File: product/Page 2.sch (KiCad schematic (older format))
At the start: 25 parts, among them J3 Conn_02x05_Odd_Even, Q1 Q_NMOS_GSD, Q2 Q_NMOS_GSD, Q3 Q_NMOS_GSD, SW1 SW_SPST, SW2 SW_SPST, U3 ESP32-WROOM-32D, X1 ECS-2520MV

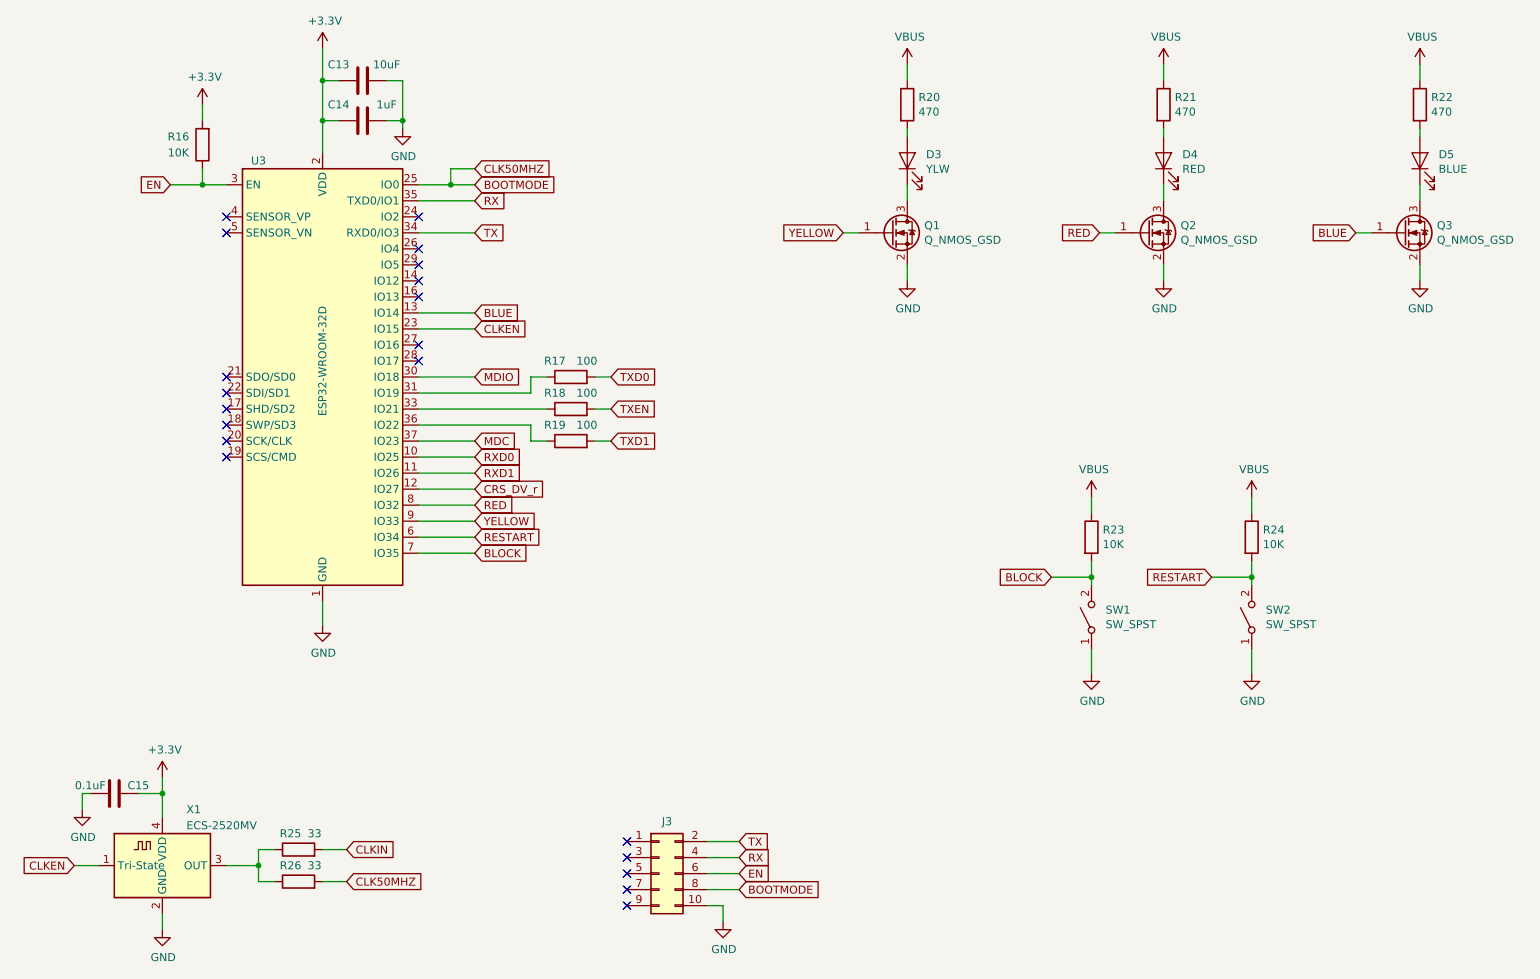
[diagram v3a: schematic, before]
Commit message: Removed oscillator, replaced with IO17
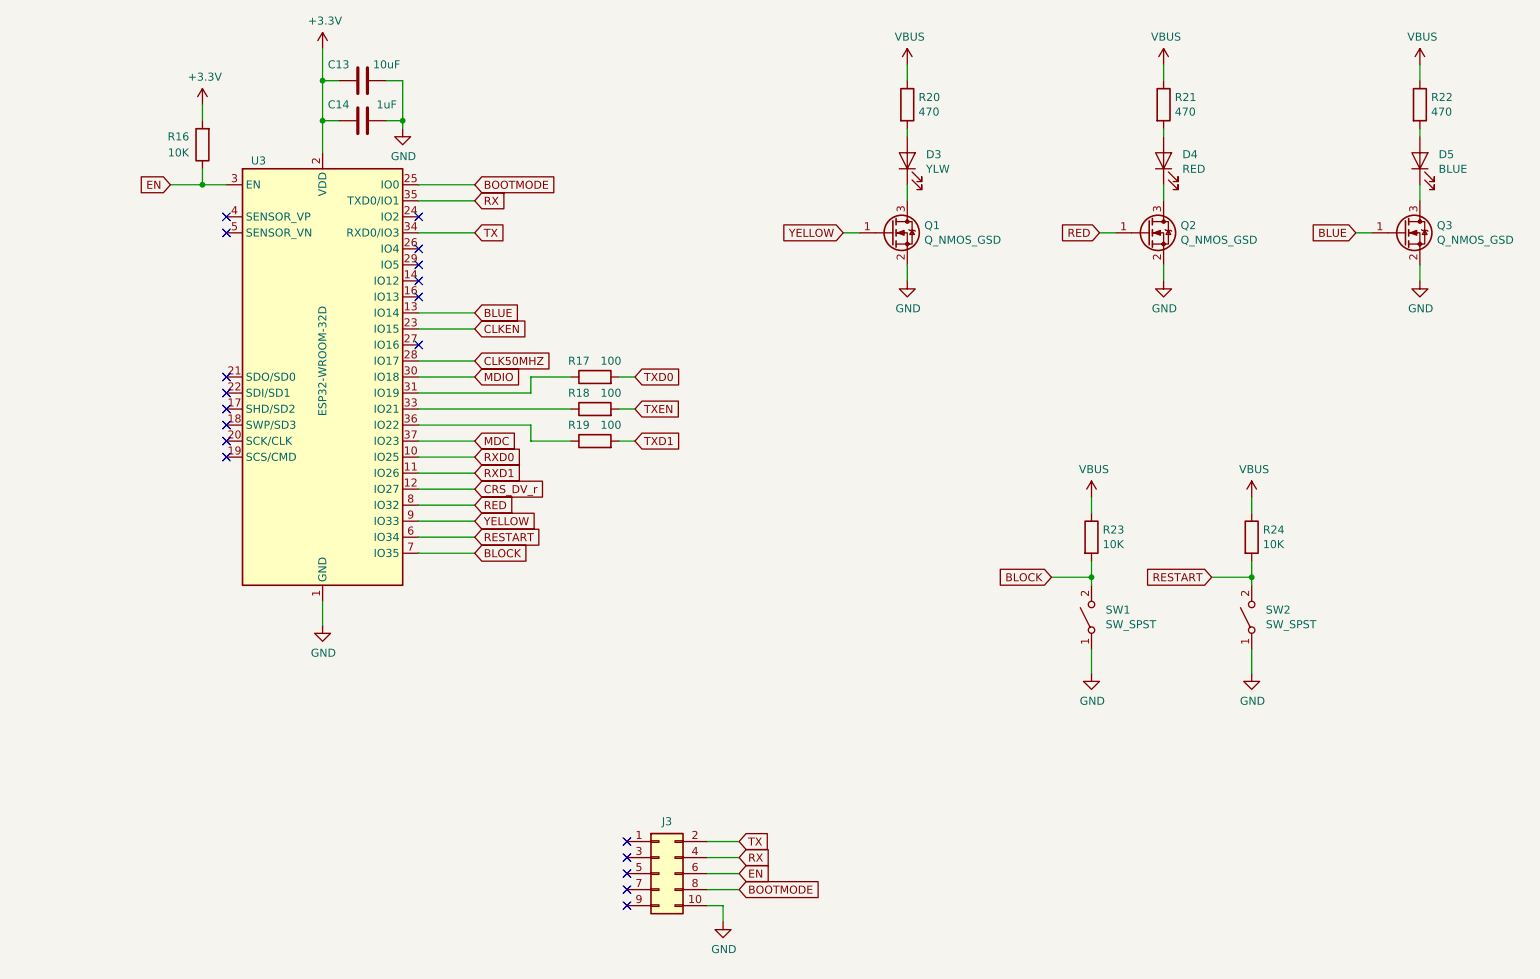
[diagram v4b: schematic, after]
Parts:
- removed C15: 0.1uF, Capacitor_SMD:C_0603_1608Metric, symbol Device:C
- removed R25, R26: 33, Resistor_SMD:R_0603_1608Metric, symbol Device:R
- removed X1: ECS-2520MV, Oscillator:Oscillator_SMD_ECS_2520MV-xxx-xx-4Pin_2.5x2.0mm, symbol Oscillator:ECS-2520MV-xxx-xx
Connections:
- net CLK50MHZ: now reaches U3.28 (IO17)
- no-connect marks 20 -> 19
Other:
- moved on the sheet: R17, R18, R19
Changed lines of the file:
@@
 $EndDescr
-$Comp
-L Oscillator:ECS-2520MV-xxx-xx X1
-U 1 1 5DF25907
-P 1900 6550
-F 0 "X1" H 2050 6900 50  0000 L CNN
-F 1 "ECS-2520MV" H 2050 6800 50  0000 L CNN
-F 2 "Oscillator:Oscillator_SMD_ECS_2520MV-xxx-xx-4Pin_2.5x2.0mm" H 2350 6200 50  0001 C CNN
-F 3 "https://www.ecsxtal.com/store/pdf/ECS-2520MV.pdf" H 1725 6675 50  0001 C CNN
-F 4 " C405472" H 1900 6550 50  0001 C CNN "LCSC Part Number"
-	1    1900 6550
-	1    0    0    -1
-$EndComp
 $Comp
 L EsperDNS-rescue:ESP32-WROOM-32D-RF_Module U3
@@
 Text GLabel 3850 4000 2    50   Input ~ 0
 RXD0
-Text GLabel 4700 3700 2    50   Input ~ 0
+Text GLabel 4850 3700 2    50   Input ~ 0
 TXEN
-Text GLabel 4700 3900 2    50   Input ~ 0
+Text GLabel 4850 3900 2    50   Input ~ 0
 TXD1
-Text GLabel 4700 3500 2    50   Input ~ 0
+Text GLabel 4850 3500 2    50   Input ~ 0
 TXD0
-Text GLabel 3050 6450 2    50   Input ~ 0
-CLKIN
 Text GLabel 3850 2400 2    50   Input ~ 0
 RX
@@
 Text GLabel 3850 2300 2    50   Input ~ 0
 BOOTMODE
-Text GLabel 3850 2200 2    50   Input ~ 0
+Text GLabel 3850 3400 2    50   Input ~ 0
 CLK50MHZ
 Text GLabel 3850 3100 2    50   Input ~ 0
@@
 L Device:R R18
 U 1 1 5DF2BBCB
-P 4450 3700
-F 0 "R18" V 4550 3800 50  0000 C CNN
-F 1 "100" V 4550 3600 50  0000 C CNN
-F 2 "Resistor_SMD:R_0603_1608Metric" V 4380 3700 50  0001 C CNN
-F 3 "~" H 4450 3700 50  0001 C CNN
-F 4 "C105588" H 4450 3700 50  0001 C CNN "LCSC Part Number"
-	1    4450 3700
+P 4600 3700
+F 0 "R18" V 4700 3800 50  0000 C CNN
+F 1 "100" V 4700 3600 50  0000 C CNN
+F 2 "Resistor_SMD:R_0603_1608Metric" V 4530 3700 50  0001 C CNN
+F 3 "~" H 4600 3700 50  0001 C CNN
+F 4 "C105588" H 4600 3700 50  0001 C CNN "LCSC Part Number"
+	1    4600 3700
 	0    -1   -1   0
 $EndComp
@@
 L Device:R R19
 U 1 1 5DF2BD63
-P 4450 3900
-F 0 "R19" V 4550 4000 50  0000 C CNN
-F 1 "100" V 4550 3800 50  0000 C CNN
-F 2 "Resistor_SMD:R_0603_1608Metric" V 4380 3900 50  0001 C CNN
-F 3 "~" H 4450 3900 50  0001 C CNN
-F 4 "C105588" H 4450 3900 50  0001 C CNN "LCSC Part Number"
-	1    4450 3900
-	0    -1   -1   0
-$EndComp
-Wire Wire Line
-	3500 2300 3700 2300
-Wire Wire Line
-	3700 2300 3700 2200
-Wire Wire Line
-	3700 2200 3850 2200
-Connection ~ 3700 2300
-Wire Wire Line
-	3700 2300 3850 2300
+P 4600 3900
+F 0 "R19" V 4700 4000 50  0000 C CNN
+F 1 "100" V 4700 3800 50  0000 C CNN
+F 2 "Resistor_SMD:R_0603_1608Metric" V 4530 3900 50  0001 C CNN
+F 3 "~" H 4600 3900 50  0001 C CNN
+F 4 "C105588" H 4600 3900 50  0001 C CNN "LCSC Part Number"
+	1    4600 3900
+	0    -1   -1   0
+$EndComp
 Wire Wire Line
 	3850 2600 3500 2600
@@
 	4200 3600 4200 3500
 Wire Wire Line
-	4200 3500 4300 3500
-Wire Wire Line
-	4300 3700 3500 3700
-Wire Wire Line
 	3500 3800 4200 3800
 Wire Wire Line
 	4200 3800 4200 3900
 Wire Wire Line
-	4200 3900 4300 3900
-Wire Wire Line
-	4600 3900 4700 3900
-Wire Wire Line
-	4600 3700 4700 3700
-Wire Wire Line
-	4700 3500 4600 3500
+	4750 3900 4850 3900
+Wire Wire Line
+	4750 3700 4850 3700
+Wire Wire Line
+	4850 3500 4750 3500
 Wire Wire Line
 	3500 3200 3850 3200
@@
 L Device:R R17
 U 1 1 5DF2A186
-P 4450 3500
-F 0 "R17" V 4550 3600 50  0000 C CNN
-F 1 "100" V 4550 3400 50  0000 C CNN
-F 2 "Resistor_SMD:R_0603_1608Metric" V 4380 3500 50  0001 C CNN
-F 3 "~" H 4450 3500 50  0001 C CNN
-F 4 "C105588" H 4450 3500 50  0001 C CNN "LCSC Part Number"
-	1    4450 3500
+P 4600 3500
+F 0 "R17" V 4700 3600 50  0000 C CNN
+F 1 "100" V 4700 3400 50  0000 C CNN
+F 2 "Resistor_SMD:R_0603_1608Metric" V 4530 3500 50  0001 C CNN
+F 3 "~" H 4600 3500 50  0001 C CNN
+F 4 "C105588" H 4600 3500 50  0001 C CNN "LCSC Part Number"
+	1    4600 3500
 	0    -1   -1   0
 $EndComp
@@
 	9450 2600 9350 2600
 $Comp
-L Device:R R25
-U 1 1 5DF75E2C
-P 2750 6450
-F 0 "R25" V 2850 6500 50  0000 C CNN
-F 1 "33" V 2850 6350 50  0000 C CNN
-F 2 "Resistor_SMD:R_0603_1608Metric" V 2680 6450 50  0001 C CNN
-F 3 "~" H 2750 6450 50  0001 C CNN
-F 4 "C417099" H 2750 6450 50  0001 C CNN "LCSC Part Number"
-	1    2750 6450
-	0    -1   -1   0
-$EndComp
-$Comp
-L Device:R R26
-U 1 1 5DF7703D
-P 2750 6650
-F 0 "R26" V 2850 6700 50  0000 C CNN
-F 1 "33" V 2850 6550 50  0000 C CNN
-F 2 "Resistor_SMD:R_0603_1608Metric" V 2680 6650 50  0001 C CNN
-F 3 "~" H 2750 6650 50  0001 C CNN
-F 4 "C417099" H 2750 6650 50  0001 C CNN "LCSC Part Number"
-	1    2750 6650
-	0    -1   -1   0
-$EndComp
-Text GLabel 3050 6650 2    50   Input ~ 0
-CLK50MHZ
-Wire Wire Line
-	2300 6550 2500 6550
-Wire Wire Line
-	2500 6550 2500 6450
-Wire Wire Line
-	2500 6450 2600 6450
-Wire Wire Line
-	2900 6450 3050 6450
-Wire Wire Line
-	3050 6650 2900 6650
-Wire Wire Line
-	2600 6650 2500 6650
-Wire Wire Line
-	2500 6650 2500 6550
-Connection ~ 2500 6550
-$Comp
-L power:GND #PWR0140
-U 1 1 5DF7E615
-P 1900 6950
-F 0 "#PWR0140" H 1900 6700 50  0001 C CNN
-F 1 "GND" H 1905 6777 50  0000 C CNN
-F 2 "" H 1900 6950 50  0001 C CNN
-F 3 "" H 1900 6950 50  0001 C CNN
-	1    1900 6950
-	1    0    0    -1
-$EndComp
-$Comp
-L power:+3.3V #PWR0141
-U 1 1 5DF7EA2D
-P 1900 6000
-F 0 "#PWR0141" H 1900 5850 50  0001 C CNN
-F 1 "+3.3V" H 1915 6173 50  0000 C CNN
-F 2 "" H 1900 6000 50  0001 C CNN
-F 3 "" H 1900 6000 50  0001 C CNN
-	1    1900 6000
-	1    0    0    -1
-$EndComp
-Wire Wire Line
-	1900 6100 1900 6000
-Wire Wire Line
-	1900 6950 1900 6850
-Wire Wire Line
-	1500 6550 1350 6550
-$Comp
 L Device:R R?
 U 1 1 5DF95691
@@
 NoConn ~ 4800 6600
 NoConn ~ 4800 6500
-Wire Wire Line
-	1750 6100 1900 6100
-Wire Wire Line
-	1900 6250 1900 6100
-Connection ~ 1900 6100
-$Comp
-L power:GND #PWR0148
-U 1 1 5E082755
-P 1400 6200
-F 0 "#PWR0148" H 1400 5950 50  0001 C CNN
-F 1 "GND" H 1405 6027 50  0000 C CNN
-F 2 "" H 1400 6200 50  0001 C CNN
-F 3 "" H 1400 6200 50  0001 C CNN
-	1    1400 6200
-	1    0    0    -1
-$EndComp
 NoConn ~ 3500 2500
 NoConn ~ 3500 2700
@@
 NoConn ~ 3500 3000
 NoConn ~ 3500 3300
-NoConn ~ 3500 3400
 Wire Wire Line
 	7450 4750 7700 4750
@@
 Wire Wire Line
 	8700 4750 8700 4800
-$Comp
-L Device:C C15
-U 1 1 5E07AF59
-P 1600 6100
-F 0 "C15" V 1650 5950 50  0000 C CNN
-F 1 "0.1uF" V 1650 6250 50  0000 C CNN
-F 2 "Capacitor_SMD:C_0603_1608Metric" H 1638 5950 50  0001 C CNN
-F 3 "~" H 1600 6100 50  0001 C CNN
-F 4 "C24452" H 1600 6100 50  0001 C CNN "LCSC Part Number"
-	1    1600 6100
-	0    -1   -1   0
-$EndComp
-Wire Wire Line
-	1450 6100 1400 6100
-Wire Wire Line
-	1400 6100 1400 6200
 $Comp
 L power:VBUS #PWR?
@@
 	1    0    0    -1
 $EndComp
-Text GLabel 1350 6550 0    50   Input ~ 0
-CLKEN
 Text GLabel 3850 3200 2    50   Input ~ 0
 CLKEN
@@
 	0    -1   -1   0
 $EndComp
+Wire Wire Line
+	3500 2300 3850 2300
+Wire Wire Line
+	3500 3400 3850 3400
+Wire Wire Line
+	3500 3700 4450 3700
+Wire Wire Line
+	4200 3500 4450 3500
+Wire Wire Line
+	4200 3900 4450 3900
 $EndSCHEMATC
